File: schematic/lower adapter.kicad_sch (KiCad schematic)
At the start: 0 parts

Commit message: schematic in process
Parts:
- added J2: Lower Adapter Function Board, symbol Connector_Generic:Conn_01x11
- added P15: Conn_01x05, symbol Connector_Generic:Conn_01x05
- added P2: Conn_01x02, symbol Connector_Generic:Conn_01x02
- added P3: Conn_01x03, symbol Connector_Generic:Conn_01x03
- added P5, P6, P7, P8: Conn_01x04, symbol Connector_Generic:Conn_01x04
- added U3: STM32F103CBTx, Package_QFP:LQFP-48_7x7mm_P0.5mm, symbol MCU_ST_STM32F1:STM32F103CBTx
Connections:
- new net: U3.23 (VSS), U3.35 (VSS), U3.47 (VSS)
- new net: U3.39 (PB3), U3.40 (PB4), U3.41 (PB5), U3.42 (PB6), U3.43 (PB7)
- new net: P6.1 (Pin_1), P7.1 (Pin_1), P8.1 (Pin_1)
- new net: P6.2 (Pin_2), P7.2 (Pin_2), P8.2 (Pin_2)
- new net: P6.3 (Pin_3), P7.3 (Pin_3), P8.3 (Pin_3)
- new net: P6.4 (Pin_4), P7.4 (Pin_4), P8.4 (Pin_4)
- new net +24V: J2.1 (Pin_1), J2.2 (Pin_2), P15.5 (Pin_5), P5.3 (Pin_3), P5.4 (Pin_4)
- new net +5C: P15.3 (Pin_3), P15.4 (Pin_4)
- new net 5 Pin Header: U3.44 (BOOT0)
- new net 5 Pin Rx/Tx: U3.31 (PA10), U3.32 (PA11)
- new net 5v out: J2.7 (Pin_7), J2.9 (Pin_9), P3.1 (Pin_1)
- new net BED_HEATER: J2.8 (Pin_8), P3.3 (Pin_3)
- new net BED_PROBE: J2.10 (Pin_10)
- new net GND: J2.11 (Pin_11), J2.3 (Pin_3), J2.4 (Pin_4), J2.5 (Pin_5), J2.6 (Pin_6), P15.1 (Pin_1), P15.2 (Pin_2), P2.1 (Pin_1), P2.2 (Pin_2), P3.2 (Pin_2), P5.1 (Pin_1), P5.2 (Pin_2)
- new net Output and LED1: U3.25 (PB12)
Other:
- note added: "1117 3v3 regulator for stm32 u6 is low drop out regulator low noise for HY717"
- note added: "Board has wifi and sd card for core board Board has a dc/dc for core board 5.2V power P15 provides 24V, 5.2V and Gnd to core board Other signals in the ribbon cable"
- note added: "Bottom via from HX717"
- note added: "Btm?? vias"
- note added: "MOS Bed Heater Power"
- note added: "Power and GND from MOS pcb"
- note added: "Strain Gauges In Parallel"
- note added: "Todo HX717 configuration and connections S0 and S1 Pullups???"
- note added: "U5 Voltage Suppervisor"
- note added: "pull down"
- title: (none) -> Lower Function Adapter Board V2.6

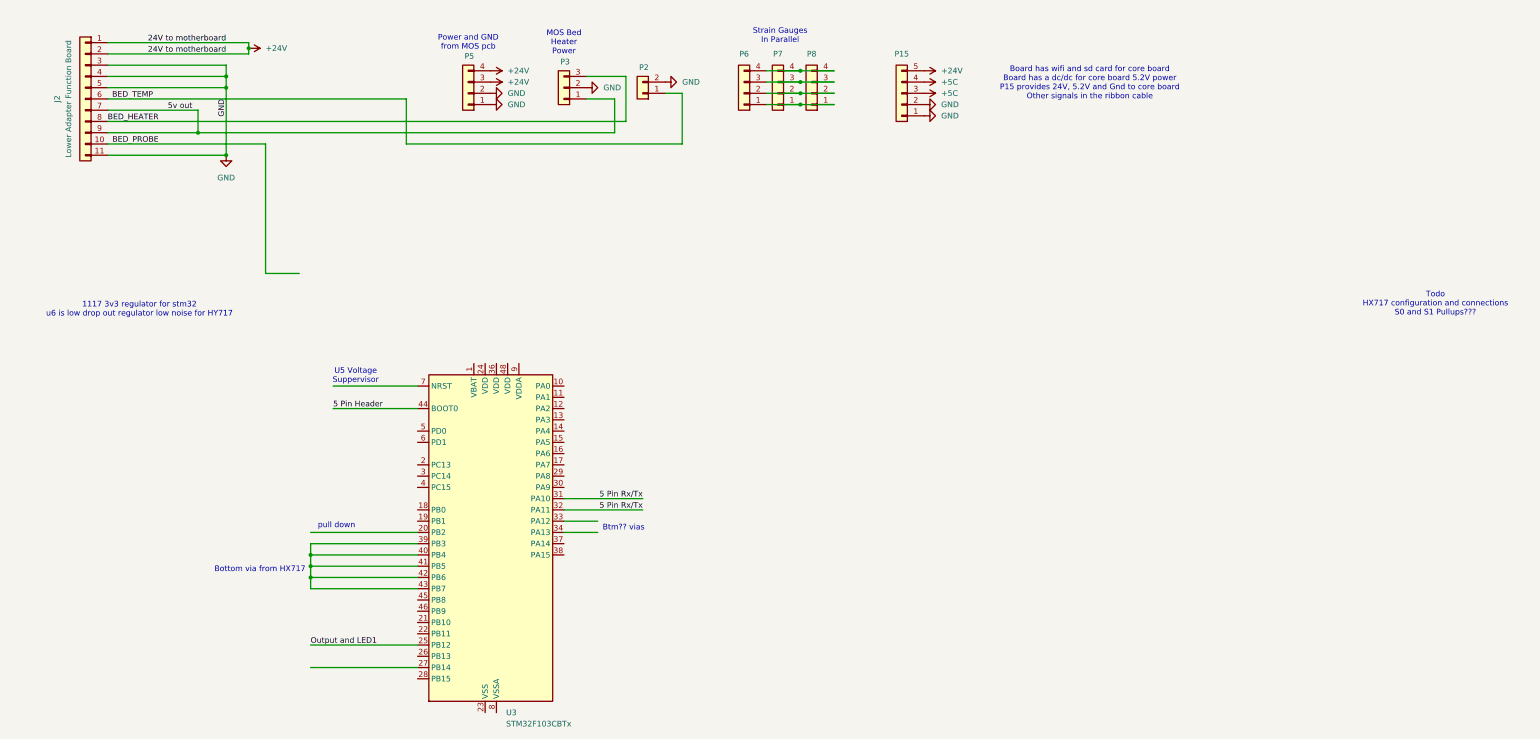
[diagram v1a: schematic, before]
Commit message: updates for load cell
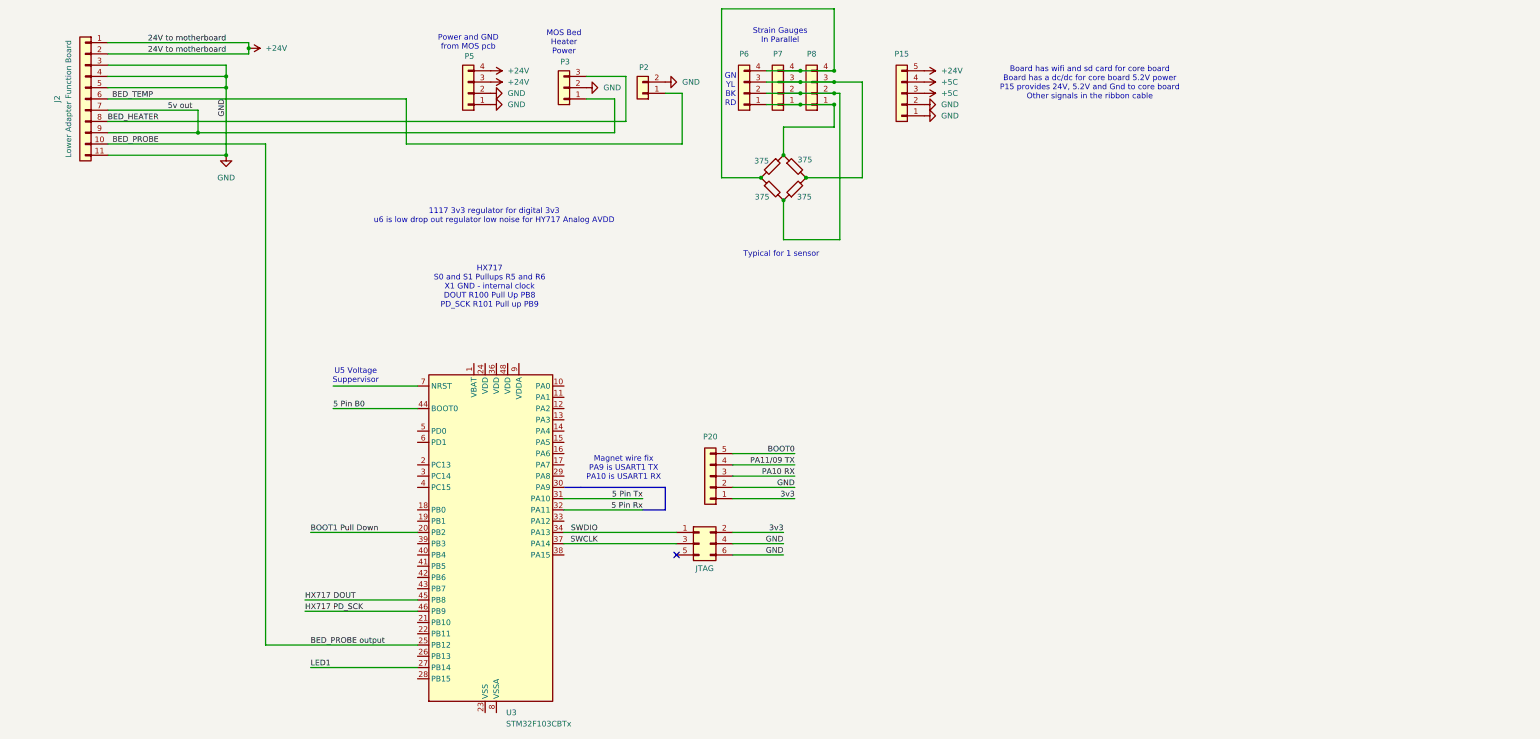
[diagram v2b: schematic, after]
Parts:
- added JTAG: Conn_02x03_Odd_Even, symbol Connector_Generic:Conn_02x03_Odd_Even
- added P20: Conn_01x05, symbol Connector_Generic:Conn_01x05
- added R1, R2, R3, R4: 375, symbol Device:R_45deg
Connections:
- net Output and LED1 is gone; now on net BED_PROBE: U3.25 (PB12)
- net GND: now also JTAG.4 (Pin_4), JTAG.6 (Pin_6), P20.2 (Pin_2)
- net BOOT1 Pull Down: now reaches U3.20 (PB2)
- net LED1: now reaches U3.27 (PB14)
- net SWDIO: now reaches U3.34 (PA13)
- net SWDIO: now also JTAG.1 (Pin_1)
- net SWCLK: now reaches U3.37 (PA14)
- net SWCLK: now also JTAG.3 (Pin_3)
- net HX717 DOUT: now reaches U3.45 (PB8)
- net HX717 PD_SCK: now reaches U3.46 (PB9)
- net at P6.1 (Pin_1), P7.1 (Pin_1), P8.1 (Pin_1): now also R2.1, R4.1
- net at P6.2 (Pin_2), P7.2 (Pin_2), P8.2 (Pin_2): now also R1.2, R3.1
- net at P6.3 (Pin_3), P7.3 (Pin_3), P8.3 (Pin_3): now also R2.2, R3.2
- net at P6.4 (Pin_4), P7.4 (Pin_4), P8.4 (Pin_4): now also R1.1, R4.2
- net 5 Pin Header renamed 5 Pin B0
- net 5 Pin Rx/Tx renamed 5 Pin Rx
- net 5 Pin Rx: no longer U3.31 (PA10)
- new net 3v3: JTAG.2 (Pin_2), P20.1 (Pin_1)
- new net 5 Pin Tx: U3.31 (PA10)
- new net BOOT0: P20.5 (Pin_5)
- new net PA10 RX: P20.3 (Pin_3)
- new net PA11/09 TX: P20.4 (Pin_4)
- now unconnected: U3.39 (PB3), U3.40 (PB4), U3.41 (PB5), U3.42 (PB6), U3.43 (PB7)
- no-connect marks 0 -> 1
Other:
- note added: "1117 3v3 regulator for digital 3v3 u6 is low drop out regulator low noise for HY717 Analog AVDD"
- note added: "GN YL BK RD"
- note added: "HX717 S0 and S1 Pullups R5 and R6 X1 GND - internal clock DOUT R100 Pull Up PB8 PD_SCK R101 Pull up PB9"
- note added: "Magnet wire fix PA9 is USART1 TX PA10 is USART1 RX"
- note added: "Typical for 1 sensor"
- note removed: "1117 3v3 regulator for stm32 u6 is low drop out regulator low noise for HY717"
- note removed: "Bottom via from HX717"
- note removed: "Btm?? vias"
- note removed: "Todo HX717 configuration and connections S0 and S1 Pullups???"
- note removed: "pull down"

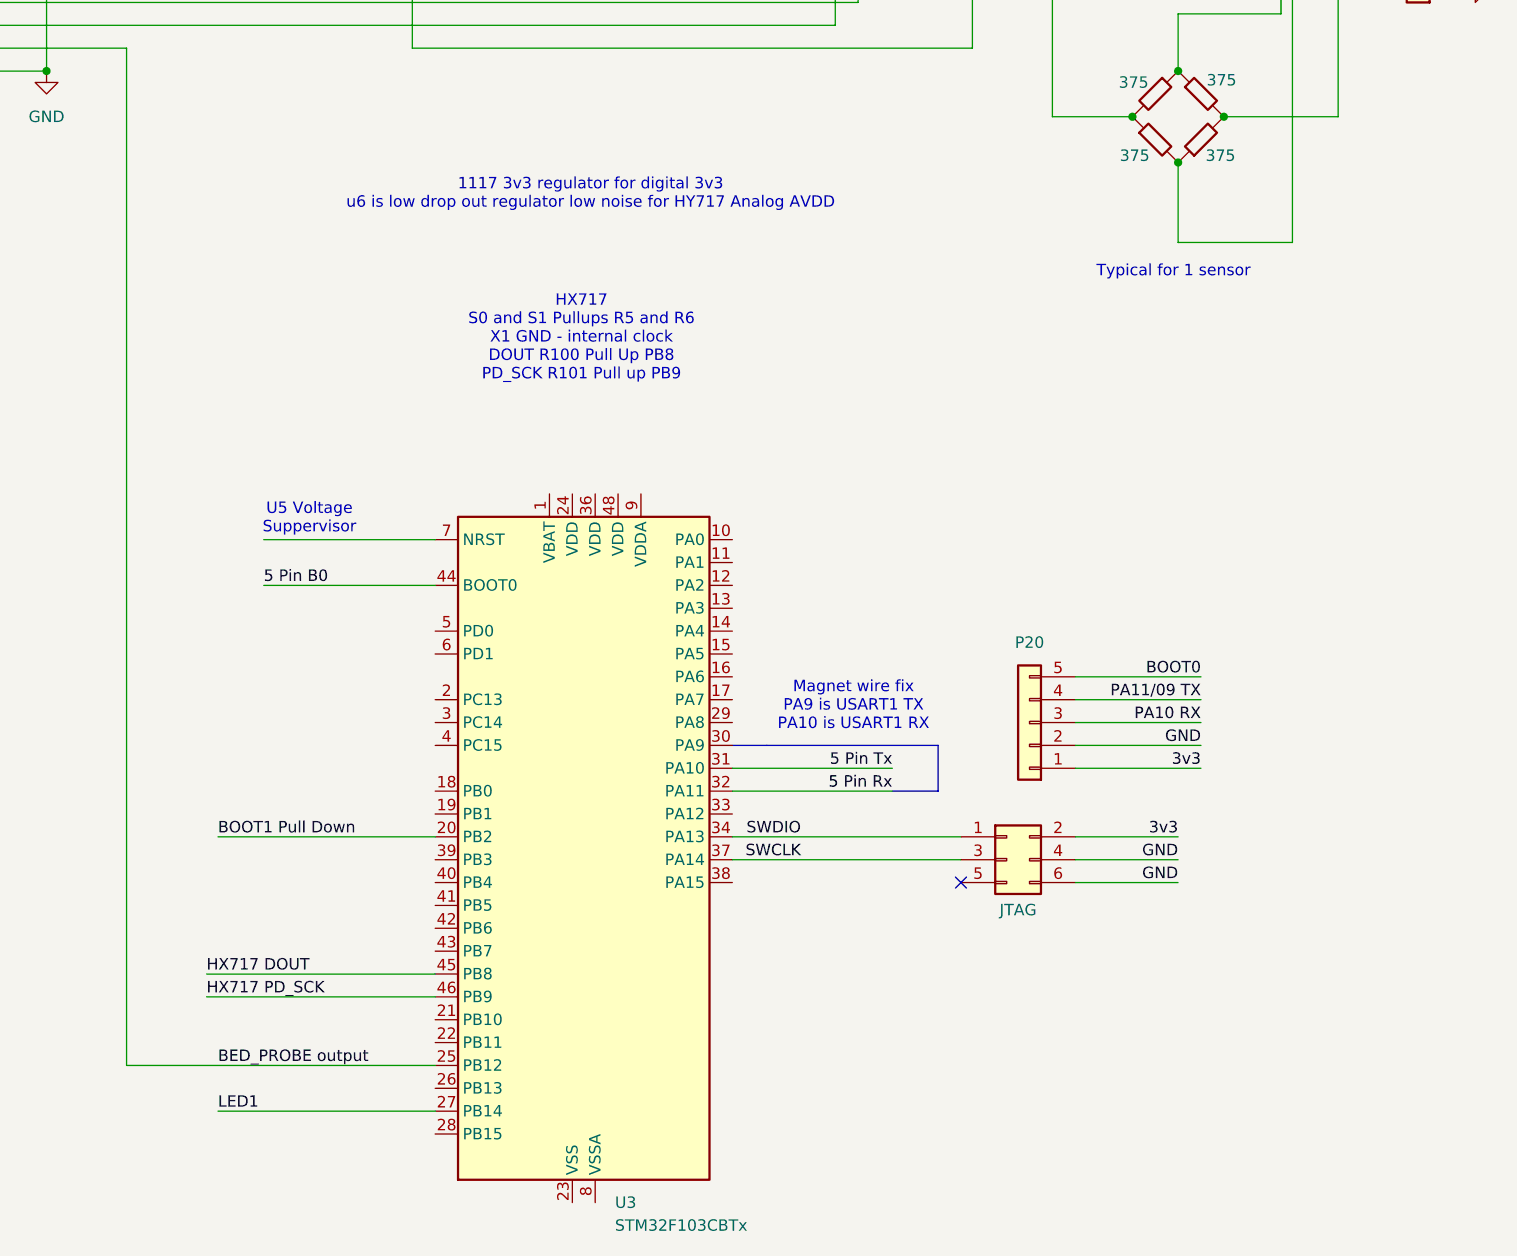
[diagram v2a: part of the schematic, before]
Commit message: revamp installation for katapult
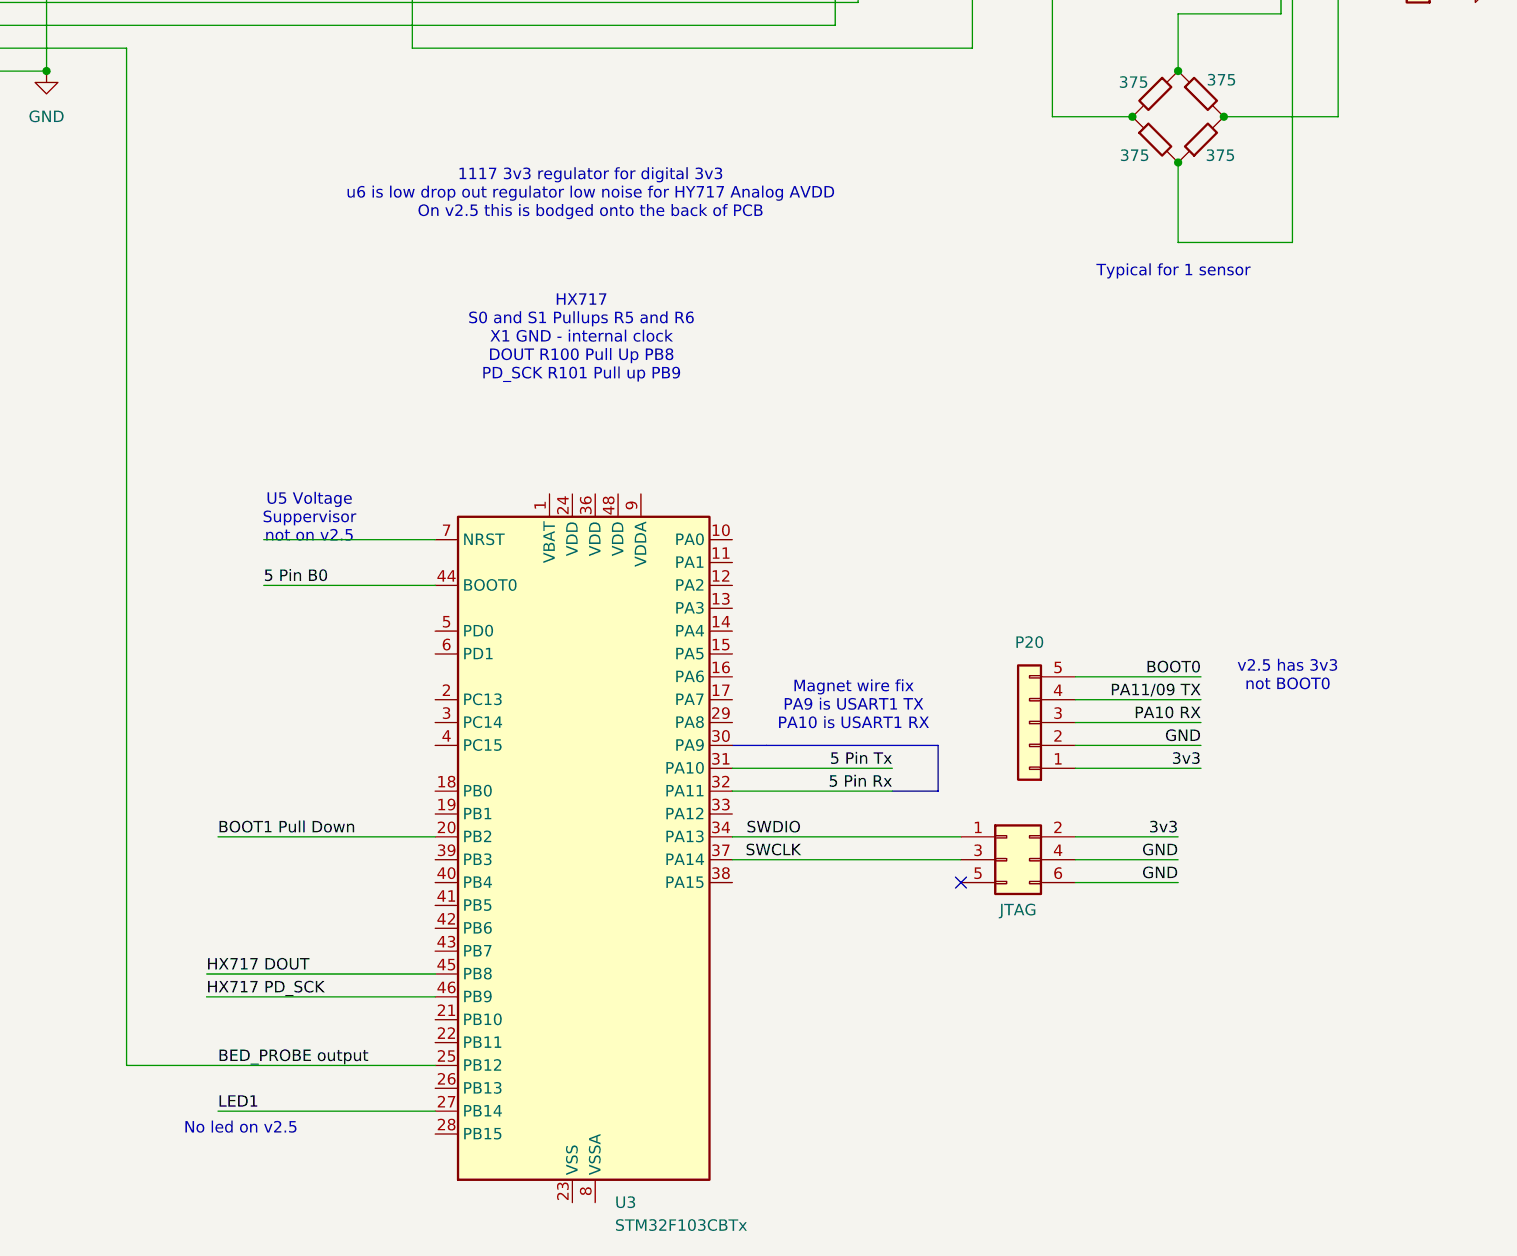
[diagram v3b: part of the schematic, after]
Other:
- note added: "1117 3v3 regulator for digital 3v3 u6 is low drop out regulator low noise for HY717 Analog AVDD On v2.5 this is bodged onto the back of PCB"
- note added: "No led on v2.5"
- note added: "U5 Voltage Suppervisor not on v2.5"
- note added: "v2.5 has 3v3 not BOOT0"
- note removed: "1117 3v3 regulator for digital 3v3 u6 is low drop out regulator low noise for HY717 Analog AVDD"
- note removed: "U5 Voltage Suppervisor"
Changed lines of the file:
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@@
 		)
 	)
-	(text "U5 Voltage \nSuppervisor\n"
+	(text "U5 Voltage \nSuppervisor\nnot on v2.5"
 		(exclude_from_sim no)
 		(at 88.9 110.744 0)
@@
 		)
 	)
+	(text "v2.5 has 3v3\nnot BOOT0"
+		(exclude_from_sim no)
+		(at 197.612 128.27 0)
+		(effects
+			(font
+				(size 1.27 1.27)
+			)
+		)
+	)
 	(text "MOS Bed\nHeater\nPower"
 		(exclude_from_sim no)
 		(at 135.89 35.56 0)
+		(effects
+			(font
+				(size 1.27 1.27)
+			)
+		)
+	)
+	(text "No led on v2.5"
+		(exclude_from_sim no)
+		(at 81.28 178.562 0)
 		(effects
 			(font
@@
 		)
 	)
-	(text "1117 3v3 regulator for digital 3v3\nu6 is low drop out regulator low noise for HY717 Analog AVDD\n"
+	(text "1117 3v3 regulator for digital 3v3\nu6 is low drop out regulator low noise for HY717 Analog AVDD\nOn v2.5 this is bodged onto the back of PCB\n"
 		(exclude_from_sim no)
 		(at 120.142 74.676 0)
